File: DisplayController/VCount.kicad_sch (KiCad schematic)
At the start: 10 parts, among them SW201 SW_DIP_x10, U202 GAL22V10, U203 74ALS163, U204 74ALS163, U205 74ALS163

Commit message: assigned footprints
Will need to double check.
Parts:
- C202, C203, C204, C205: footprint (none) -> Capacitor_SMD:C_0805_2012Metric_Pad1.18x1.45mm_HandSolder
- SW201: footprint (none) -> Package_DIP:DIP-20_W7.62mm
- U202: footprint (none) -> Package_DIP:DIP-24_W7.62mm_Socket
- U203, U204, U205: footprint (none) -> Package_SO:SOIC-16W_5.3x10.2mm_P1.27mm
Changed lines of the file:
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@@
 			)
 		)
-		(property "Footprint" ""
+		(property "Footprint" "Package_SO:SOIC-16W_5.3x10.2mm_P1.27mm"
 			(at 158.75 83.82 0)
 			(effects
@@
 			)
 		)
-		(property "Footprint" ""
+		(property "Footprint" "Capacitor_SMD:C_0805_2012Metric_Pad1.18x1.45mm_HandSolder"
 			(at 70.8152 35.56 0)
 			(effects
@@
 			)
 		)
-		(property "Footprint" ""
+		(property "Footprint" "Package_SO:SOIC-16W_5.3x10.2mm_P1.27mm"
 			(at 55.88 83.82 0)
 			(effects
@@
 			)
 		)
-		(property "Footprint" ""
+		(property "Footprint" "Package_DIP:DIP-20_W7.62mm"
 			(at 40.64 173.99 0)
 			(effects
@@
 			)
 		)
-		(property "Footprint" ""
+		(property "Footprint" "Capacitor_SMD:C_0805_2012Metric_Pad1.18x1.45mm_HandSolder"
 			(at 25.7302 35.56 0)
 			(effects
@@
 			)
 		)
-		(property "Footprint" ""
+		(property "Footprint" "Package_DIP:DIP-24_W7.62mm_Socket"
 			(at 223.52 100.33 0)
 			(effects
@@
 			)
 		)
-		(property "Footprint" ""
+		(property "Footprint" "Package_SO:SOIC-16W_5.3x10.2mm_P1.27mm"
 			(at 106.68 83.82 0)
 			(effects
@@
 			)
 		)
-		(property "Footprint" ""
+		(property "Footprint" "Capacitor_SMD:C_0805_2012Metric_Pad1.18x1.45mm_HandSolder"
 			(at 55.5752 35.56 0)
 			(effects
@@
 			)
 		)
-		(property "Footprint" ""
+		(property "Footprint" "Capacitor_SMD:C_0805_2012Metric_Pad1.18x1.45mm_HandSolder"
 			(at 40.9702 35.56 0)
 			(effects

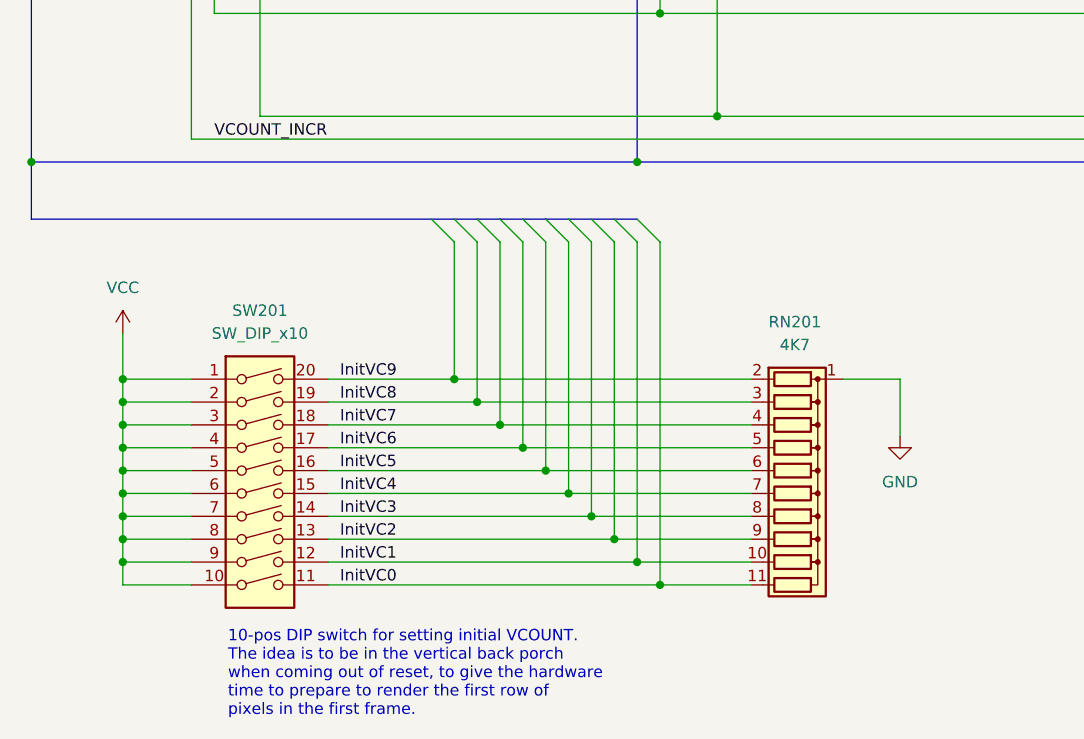
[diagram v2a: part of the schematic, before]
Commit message: eliminate DIP switch for initial VCOUNT
Instead, hard-code initial VCOUNT to 485 (which is
what the prototype sets it to.) This ensures that
a VSync pulse clears the row begin address register
before the first visible frame.
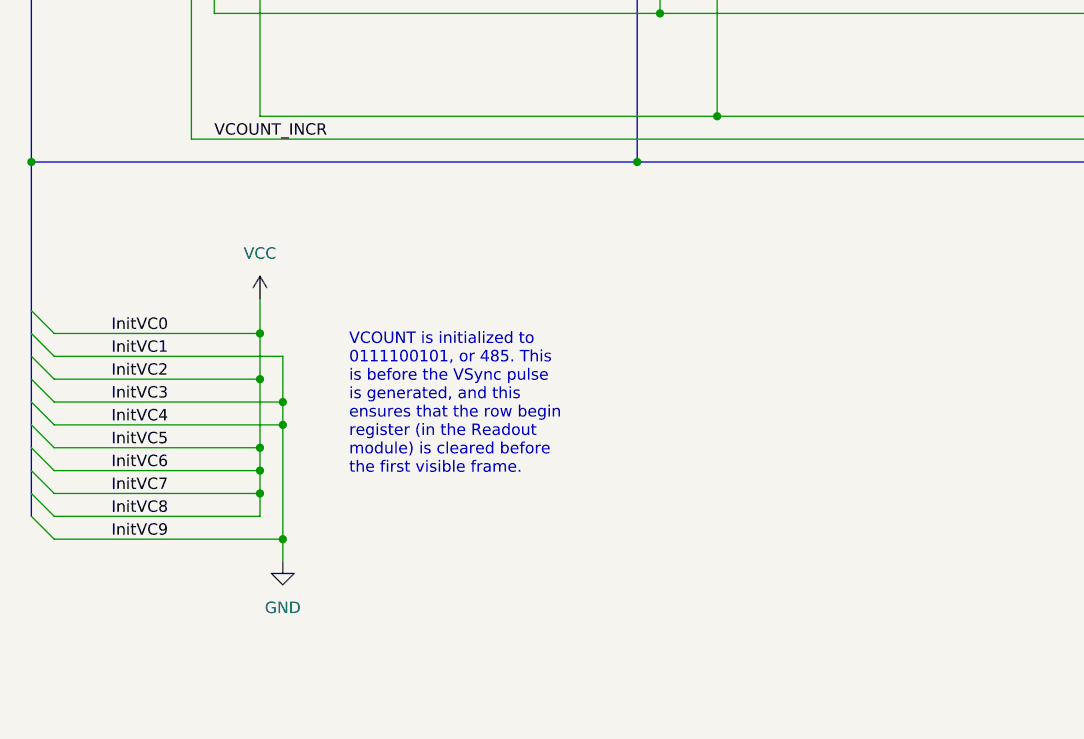
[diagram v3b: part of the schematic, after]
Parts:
- removed RN201: 4K7, Resistor_THT:R_Array_SIP11, symbol Device:R_Network10
- removed SW201: SW_DIP_x10, Package_DIP:DIP-20_W7.62mm, symbol Switch:SW_DIP_x10
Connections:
- net InitVC0 is gone; now on net VCC: U203.3 (D0)
- net InitVC1 is gone; now on net GND: U203.4 (D1)
- net InitVC2 is gone; now on net VCC: U203.5 (D2)
- net InitVC3 is gone; now on net GND: U203.6 (D3)
- net InitVC4 is gone; now on net GND: U204.3 (D0)
- net InitVC5 is gone; now on net VCC: U204.4 (D1)
- net InitVC6 is gone; now on net VCC: U204.5 (D2)
- net InitVC7 is gone; now on net VCC: U204.6 (D3)
- net InitVC8 is gone; now on net VCC: U205.3 (D0)
- net InitVC9 is gone; now on net GND: U205.4 (D1)
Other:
- note added: "VCOUNT is initialized to 0111100101, or 485. This is before the VSync pulse is generated, and this ensures that the row begin register (in the Readout module) is cleared before the first visible frame."
- note removed: "10-pos DIP switch for setting initial VCOUNT. The idea is to be in the vertical back porch when coming out of reset, to give the hardware time to prepare to render the first row of pixels in the first frame."

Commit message: initial PCB component placement
Changed package for GAL22V10 to SOIC24 rather than DIP24.
That means we'll use ATF22V10C parts (which are available
as SOIC24.)

Now for the routing :-)
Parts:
- U202: footprint Package_DIP:DIP-24_W7.62mm_Socket -> Package_SO:SOIC-24W_7.5x15.4mm_P1.27mm
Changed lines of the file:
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@@
 			)
 		)
-		(property "Footprint" "Package_DIP:DIP-24_W7.62mm_Socket"
+		(property "Footprint" "Package_SO:SOIC-24W_7.5x15.4mm_P1.27mm"
 			(at 223.52 100.33 0)
 			(effects
